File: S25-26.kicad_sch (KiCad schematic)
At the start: 117 parts, among them IC1 CMV4000-3E5M0PN, IC10 MT29F2G01ABAGDWB-IT_G_TR, IC13 DS90LV011AHMF_NOPB, IC2 XMC7200D-E272K8384AA, IC3 DS90LV048ATM_NOPB, IC4 DS90LV048ATM_NOPB, IC5 DS90LV048ATM_NOPB, IC6 NCV317BD2TR4G, IC7 MXL86110I-AQB-R, IC9 MT29F2G01ABAGDWB-IT_G_TR, Q2 ZXT849K, U1 TPS73601DBV, U2 TPS73601DBV, Y1 DSC1101DM2-012.0000

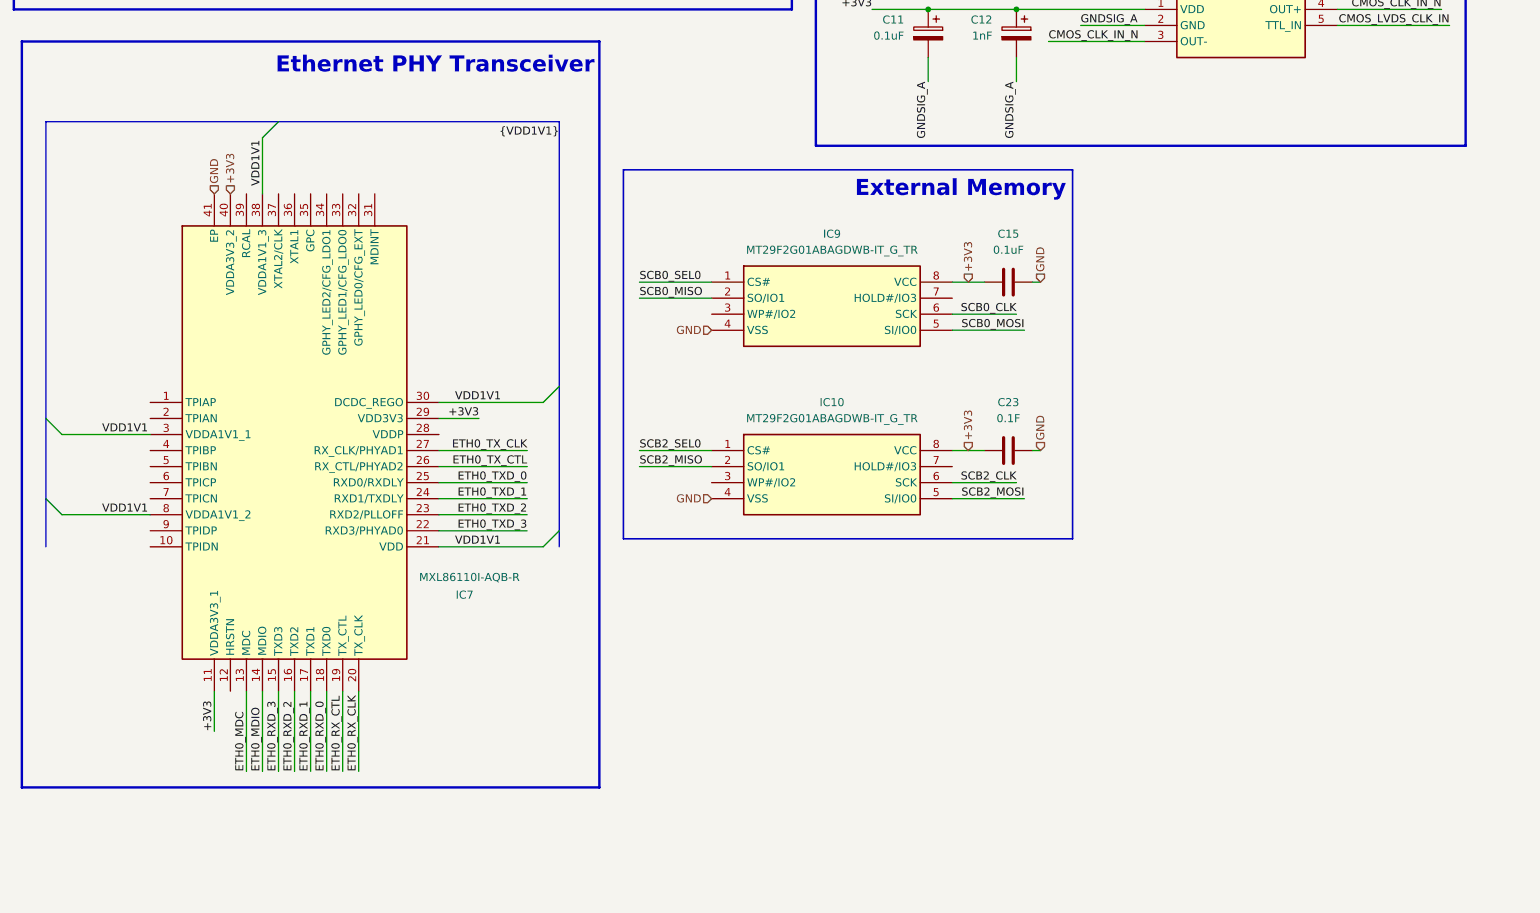
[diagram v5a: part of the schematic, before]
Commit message: Add some preliminary pin connectors and RJ45; fix some ethernet phy connections
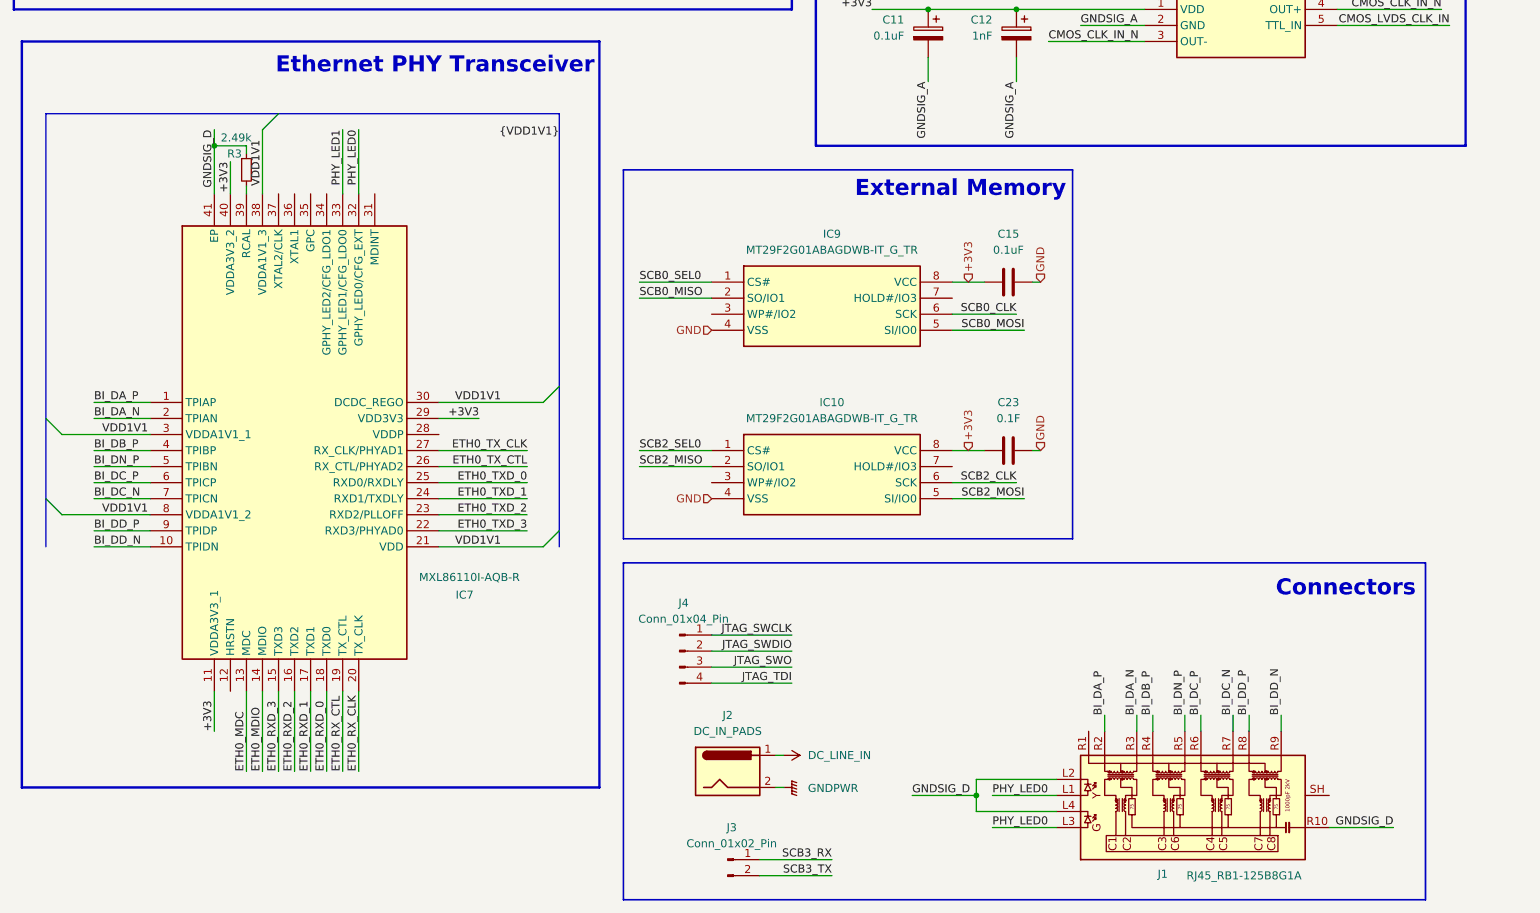
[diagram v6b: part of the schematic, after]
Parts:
- added J1: RJ45_RB1-125B8G1A, Connector_RJ:RJ45_UDE_RB1-125B8G1A, symbol Connector:RJ45_RB1-125B8G1A
- added J2: DC_IN_PADS, Connector_Wire:SolderWire-0.1sqmm_1x02_P3.6mm_D0.4mm_OD1mm_Relief, symbol Connector:Barrel_Jack
- added J3: Conn_01x02_Pin, Connector:JWT_A3963_1x02_P3.96mm_Vertical, symbol Connector:Conn_01x02_Pin
- added J4: Conn_01x04_Pin, symbol Connector:Conn_01x04_Pin
- added R3: 2.49k, symbol Device:R_Small
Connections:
- net DC_LINE_IN: now also J2.1
- net GND: no longer IC7.41 (EP)
- net GNDPWR: now also J2.2
- net GNDSIG_D: now also IC7.41 (EP), J1.L2, J1.L4, J1.R10 (GND), R3.1
- net JTAG_SWCLK: now also J4.1 (Pin_1)
- net JTAG_SWDIO: now also J4.2 (Pin_2)
- net JTAG_SWO: now also J4.3 (Pin_3)
- net JTAG_TDI: now also J4.4 (Pin_4)
- net SCB3_RX: now also J3.1 (Pin_1)
- net SCB3_TX: now also J3.2 (Pin_2)
- net BI_DA_P: now reaches IC7.1 (TPIAP)
- net BI_DA_P: now also J1.R2 (TD1+)
- net BI_DD_N: now reaches IC7.10 (TPIDN)
- net BI_DD_N: now also J1.R9 (TD4-)
- net BI_DA_N: now reaches IC7.2 (TPIAN)
- net BI_DA_N: now also J1.R3 (TD1-)
- net PHY_LED0: now reaches IC7.32 (GPHY_LED0/CFG_EXT)
- net PHY_LED0: now also J1.L1, J1.L3
- net PHY_LED1: now reaches IC7.33 (GPHY_LED1/CFG_LDO0)
- net at IC7.39 (RCAL): now also R3.2
- net BI_DB_P: now reaches IC7.4 (TPIBP)
- net BI_DB_P: now also J1.R4 (TD2+)
- net BI_DN_P: now reaches IC7.5 (TPIBN)
- net BI_DN_P: now also J1.R5 (TD2-)
- net BI_DC_P: now reaches IC7.6 (TPICP)
- net BI_DC_P: now also J1.R6 (TD3+)
- net BI_DC_N: now reaches IC7.7 (TPICN)
- net BI_DC_N: now also J1.R7 (TD3-)
- net BI_DD_P: now reaches IC7.9 (TPIDP)
- net BI_DD_P: now also J1.R8 (TD4+)
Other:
- note added: "Connectors"
